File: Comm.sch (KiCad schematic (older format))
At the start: 12 parts

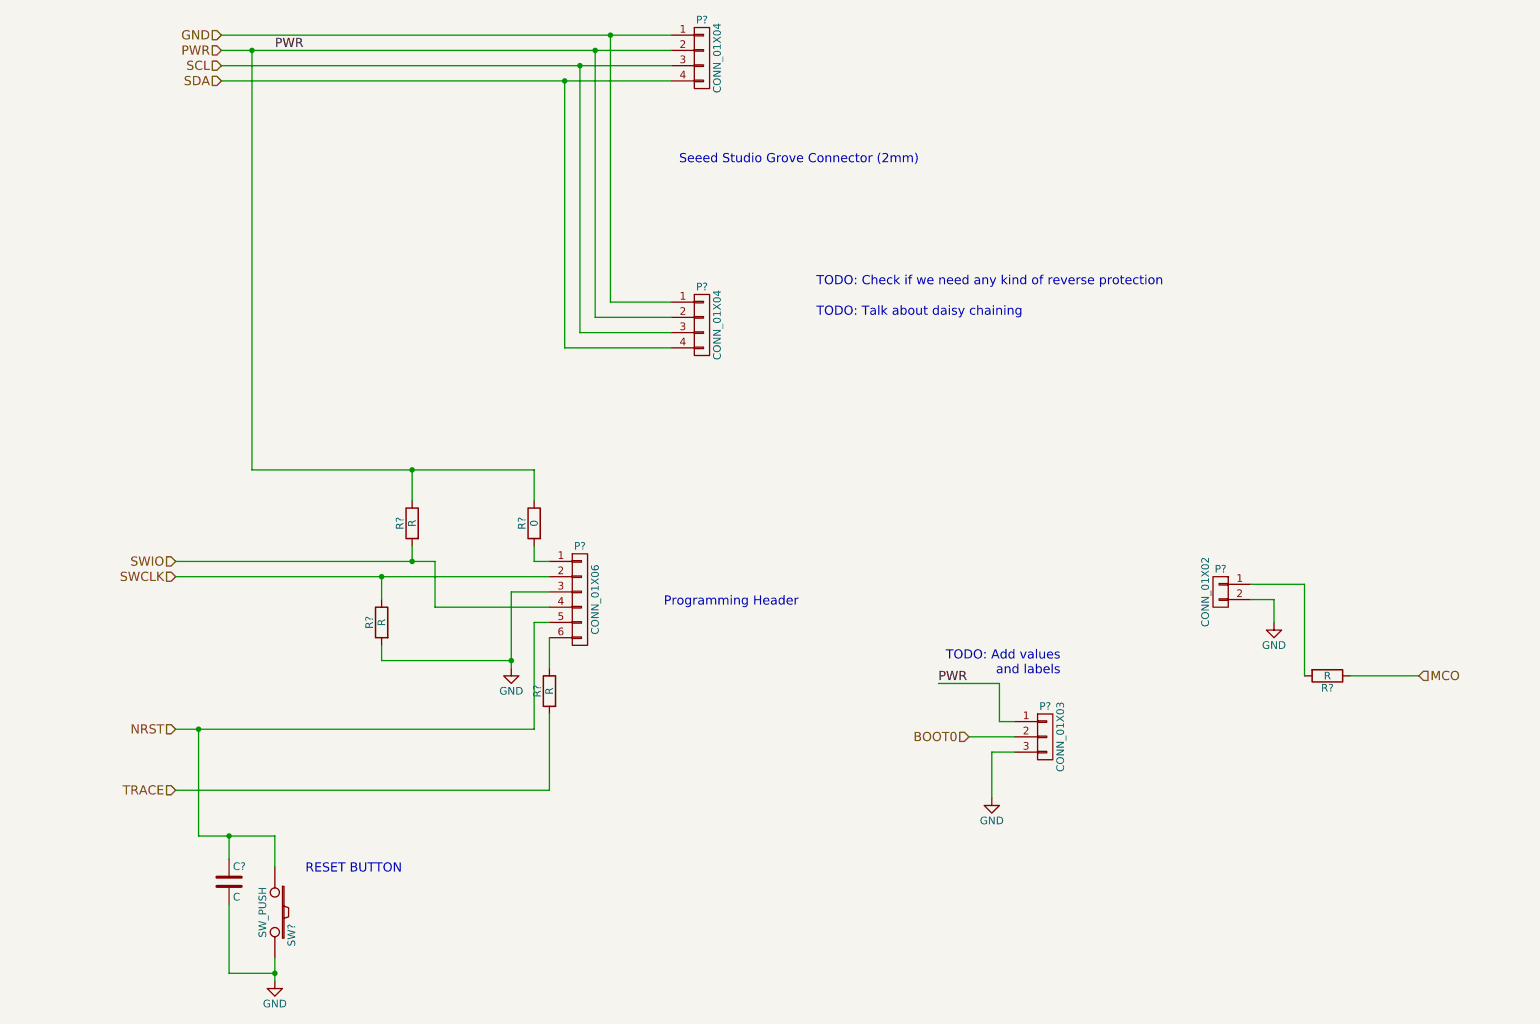
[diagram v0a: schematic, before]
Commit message: Associated footprints, created footprints for 2mm connector and did prelim placement
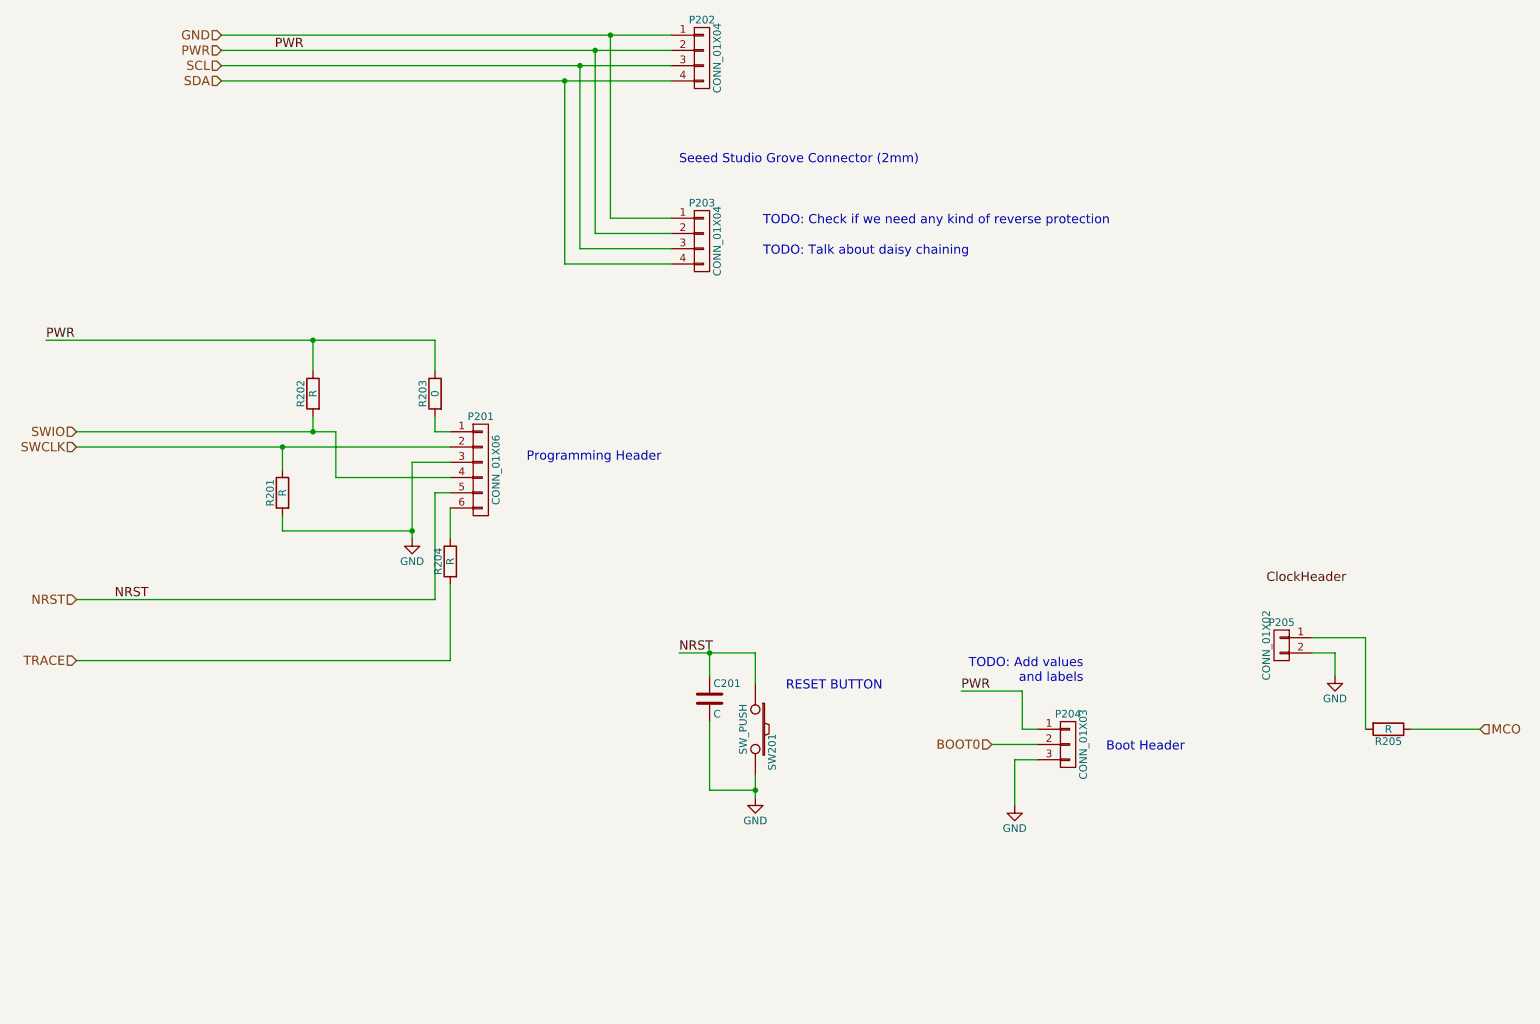
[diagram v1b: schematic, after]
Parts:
- C201: renamed from C?; footprint (none) -> Capacitors_SMD:C_0805
- P202, P203: renamed from P?; footprint (none) -> CentralCommand:Grove-2mm
- P204: renamed from P?; footprint (none) -> Pin_Headers:Pin_Header_Straight_1x03
- SW201: renamed from SW?; footprint (none) -> Buttons_Switches_ThroughHole:SW_PUSH_SMALL
- gave numbers to parts that had none: 7
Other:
- note added: "Boot Header"
- moved on the sheet: C201, P201, P203, P204, P205, R201, R202, R203, R204, R205, SW201

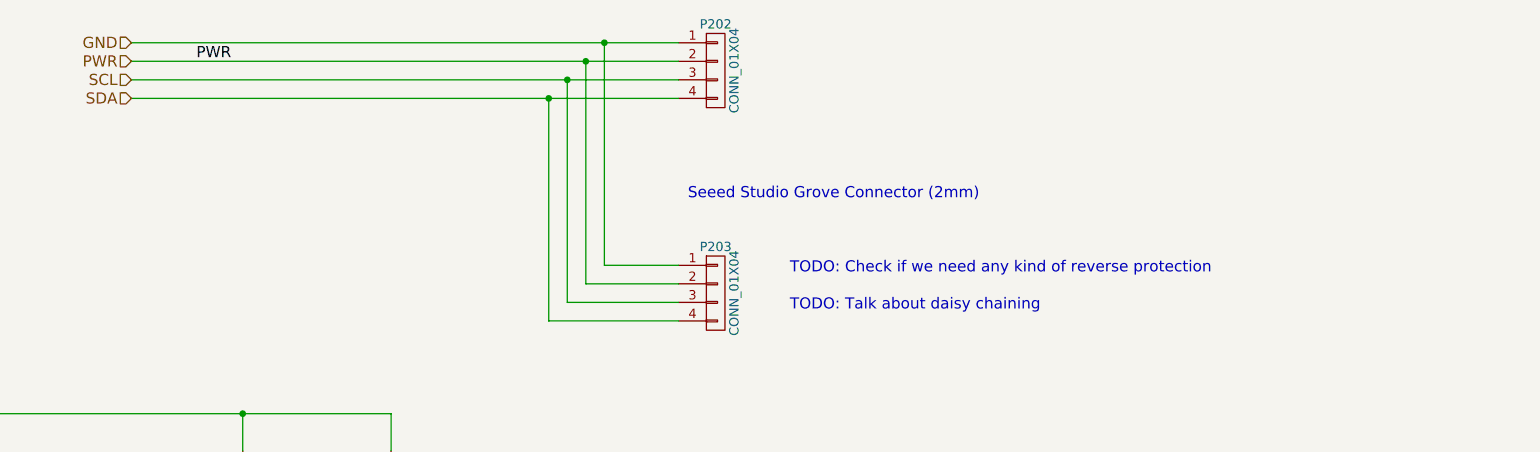
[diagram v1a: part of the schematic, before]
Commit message: Swapped connections on the Grove connector
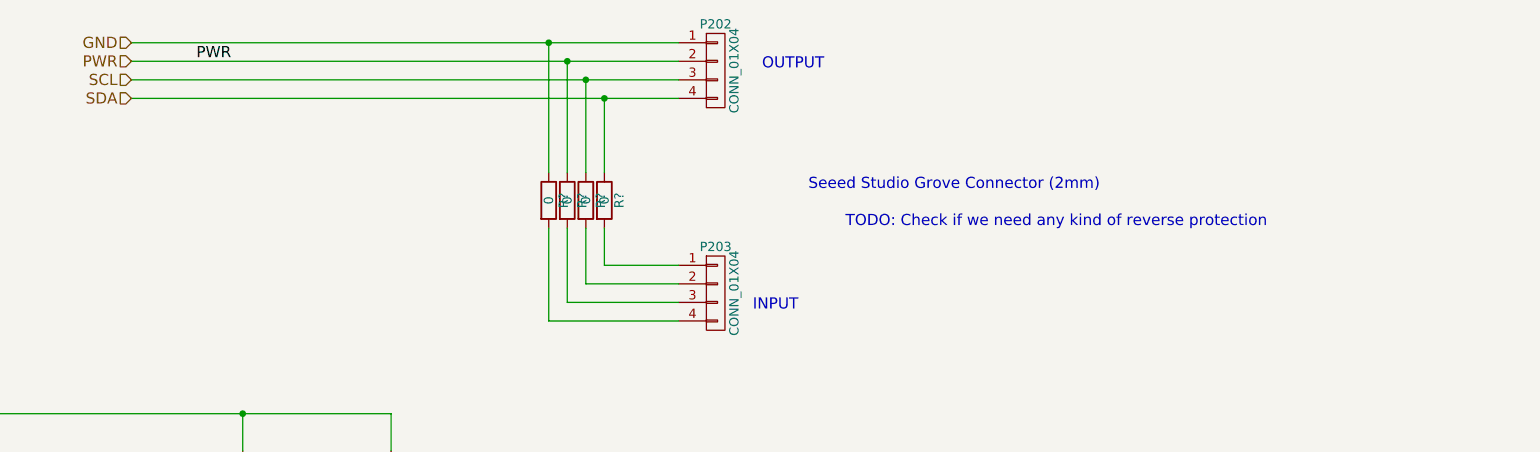
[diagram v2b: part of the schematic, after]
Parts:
- added R? (x4): 0, symbol R
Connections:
- net GND: now also R?.1; no longer P203.1 (P1)
- net PWR: now also R?.1; no longer P203.2 (P2)
- net SCL: now also R?.1; no longer P203.3 (P3)
- net SDA: now also R?.1; no longer P203.4 (P4)
- new net: P203.1 (P1), R?.2
- new net: P203.2 (P2), R?.2
- new net: P203.3 (P3), R?.2
- new net: P203.4 (P4), R?.2
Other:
- note added: "INPUT"
- note added: "OUTPUT"
- note removed: "TODO: Talk about daisy chaining"
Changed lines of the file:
@@
 SDA
 Wire Wire Line
-	2250 1500 5200 1500
-Wire Wire Line
-	2250 1400 5200 1400
-Wire Wire Line
-	2250 1300 5200 1300
-Wire Wire Line
-	2250 1200 5200 1200
-Wire Wire Line
-	4800 1200 4800 2400
-Wire Wire Line
 	4800 2400 5200 2400
-Connection ~ 4800 1200
-Wire Wire Line
-	4700 1300 4700 2500
 Wire Wire Line
 	4700 2500 5200 2500
-Connection ~ 4700 1300
-Wire Wire Line
-	4600 1400 4600 2600
 Wire Wire Line
 	4600 2600 5200 2600
-Connection ~ 4600 1400
 Wire Wire Line
 	5200 2700 4500 2700
-Wire Wire Line
-	4500 2700 4500 1500
-Connection ~ 4500 1500
-Text Notes 5250 2050 0    60   ~ 0
+Text Notes 5900 2000 0    60   ~ 0
 Seeed Studio Grove Connector (2mm)
-Text Notes 5800 2450 0    60   ~ 0
+Text Notes 6100 2200 0    60   ~ 0
 TODO: Check if we need any kind of reverse protection
-Text Notes 5800 2650 0    60   ~ 0
-TODO: Talk about daisy chaining
 $Comp
 L CONN_01X06 P201
@@
 Text Label 9100 4800 0    60   ~ 0
 ClockHeader
+Wire Wire Line
+	5200 1200 2250 1200
+Wire Wire Line
+	2250 1300 5200 1300
+Wire Wire Line
+	5200 1400 2250 1400
+Wire Wire Line
+	2250 1500 5200 1500
+$Comp
+L R R?
+U 1 1 56691488
+P 4800 2050
+F 0 "R?" V 4880 2050 50  0000 C CNN
+F 1 "0" V 4800 2050 50  0000 C CNN
+F 2 "" V 4730 2050 30  0000 C CNN
+F 3 "" H 4800 2050 30  0000 C CNN
+	1    4800 2050
+	1    0    0    -1
+$EndComp
+Wire Wire Line
+	4800 2200 4800 2400
+Wire Wire Line
+	4800 1900 4800 1500
+Connection ~ 4800 1500
+$Comp
+L R R?
+U 1 1 566915C1
+P 4700 2050
+F 0 "R?" V 4780 2050 50  0000 C CNN
+F 1 "0" V 4700 2050 50  0000 C CNN
+F 2 "" V 4630 2050 30  0000 C CNN
+F 3 "" H 4700 2050 30  0000 C CNN
+	1    4700 2050
+	1    0    0    -1
+$EndComp
+Wire Wire Line
+	4700 2500 4700 2200
+$Comp
+L R R?
+U 1 1 56691697
+P 4600 2050
+F 0 "R?" V 4680 2050 50  0000 C CNN
+F 1 "0" V 4600 2050 50  0000 C CNN
+F 2 "" V 4530 2050 30  0000 C CNN
+F 3 "" H 4600 2050 30  0000 C CNN
+	1    4600 2050
+	1    0    0    -1
+$EndComp
+Wire Wire Line
+	4600 2600 4600 2200
+Wire Wire Line
+	4600 1900 4600 1300
+Connection ~ 4600 1300
+Wire Wire Line
+	4700 1900 4700 1400
+Connection ~ 4700 1400
+$Comp
+L R R?
+U 1 1 56691864
+P 4500 2050
+F 0 "R?" V 4580 2050 50  0000 C CNN
+F 1 "0" V 4500 2050 50  0000 C CNN
+F 2 "" V 4430 2050 30  0000 C CNN
+F 3 "" H 4500 2050 30  0000 C CNN
+	1    4500 2050
+	1    0    0    -1
+$EndComp
+Wire Wire Line
+	4500 2700 4500 2200
+Wire Wire Line
+	4500 1900 4500 1200
+Connection ~ 4500 1200
+Text Notes 5650 1350 0    60   ~ 0
+OUTPUT
+Text Notes 5600 2650 0    60   ~ 0
+INPUT
 $EndSCHEMATC

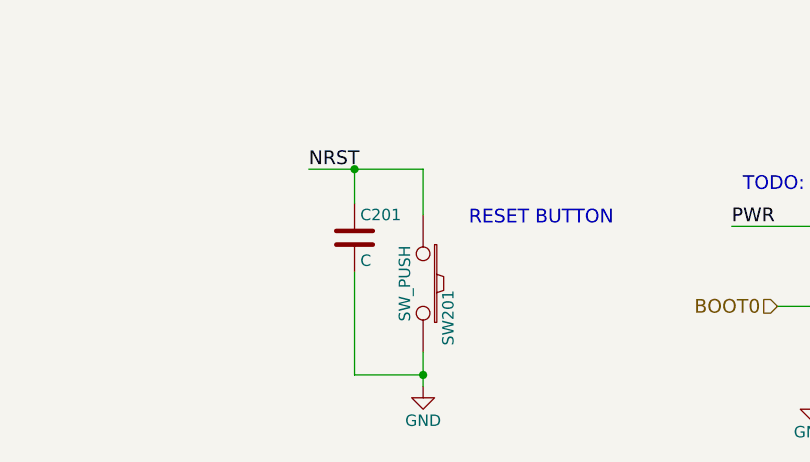
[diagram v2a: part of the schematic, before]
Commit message: Added ground and power layers.
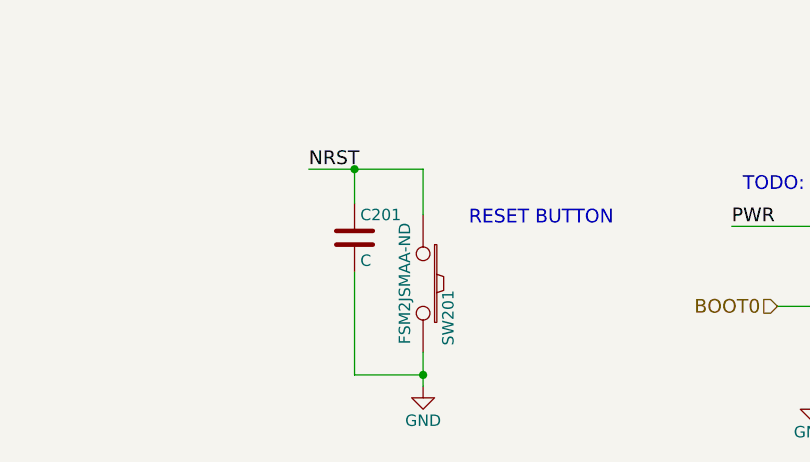
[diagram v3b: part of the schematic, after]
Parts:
- SW201: value SW_PUSH -> FSM2JSMAA-ND
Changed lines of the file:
@@
 P 5750 5750
 F 0 "SW201" H 5900 5860 50  0000 C CNN
-F 1 "SW_PUSH" H 5750 5670 50  0000 C CNN
+F 1 "FSM2JSMAA-ND" H 5750 5670 50  0000 C CNN
 F 2 "Buttons_Switches_ThroughHole:SW_PUSH_SMALL" H 5750 5750 60  0001 C CNN
-F 3 "" H 5750 5750 60  0000 C CNN
+F 3 "http://www.digikey.com/product-detail/en/FSM2JSMAA/FSM2JSMAA-ND/2400228" H 5750 5750 60  0001 C CNN
 	1    5750 5750
 	0    1    1    0

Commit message: Finished laying out power section
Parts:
- R206, R207, R208, R209: renamed from R?; footprint (none) -> Resistors_SMD:R_0805
- SW201: footprint Buttons_Switches_ThroughHole:SW_PUSH_SMALL -> CentralCommand:FSM2JSMAA-ND
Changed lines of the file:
@@
 $EndComp
 $Comp
-L GND #PWR04
+L GND #PWR05
 U 1 1 565FC7CA
 P 3500 4500
-F 0 "#PWR04" H 3500 4250 50  0001 C CNN
+F 0 "#PWR05" H 3500 4250 50  0001 C CNN
 F 1 "GND" H 3500 4350 50  0000 C CNN
 F 2 "" H 3500 4500 60  0000 C CNN
@@
 F 0 "SW201" H 5900 5860 50  0000 C CNN
 F 1 "FSM2JSMAA-ND" H 5750 5670 50  0000 C CNN
-F 2 "Buttons_Switches_ThroughHole:SW_PUSH_SMALL" H 5750 5750 60  0001 C CNN
+F 2 "CentralCommand:FSM2JSMAA-ND" H 5750 5750 60  0001 C CNN
 F 3 "http://www.digikey.com/product-detail/en/FSM2JSMAA/FSM2JSMAA-ND/2400228" H 5750 5750 60  0001 C CNN
 	1    5750 5750
@@
 $EndComp
 $Comp
-L GND #PWR05
+L GND #PWR06
 U 1 1 565FED52
 P 5750 6200
-F 0 "#PWR05" H 5750 5950 50  0001 C CNN
+F 0 "#PWR06" H 5750 5950 50  0001 C CNN
 F 1 "GND" H 5750 6050 50  0000 C CNN
 F 2 "" H 5750 6200 60  0000 C CNN
@@
 $EndComp
 $Comp
-L GND #PWR06
+L GND #PWR07
 U 1 1 5660DBDE
 P 9550 5400
-F 0 "#PWR06" H 9550 5150 50  0001 C CNN
+F 0 "#PWR07" H 9550 5150 50  0001 C CNN
 F 1 "GND" H 9550 5250 50  0000 C CNN
 F 2 "" H 9550 5400 60  0000 C CNN
@@
 	7450 5950 7450 6250
 $Comp
-L GND #PWR07
+L GND #PWR08
 U 1 1 5661772D
 P 7450 6250
-F 0 "#PWR07" H 7450 6000 50  0001 C CNN
+F 0 "#PWR08" H 7450 6000 50  0001 C CNN
 F 1 "GND" H 7450 6100 50  0000 C CNN
 F 2 "" H 7450 6250 60  0000 C CNN
@@
 	2250 1500 5200 1500
 $Comp
-L R R?
+L R R209
 U 1 1 56691488
 P 4800 2050
-F 0 "R?" V 4880 2050 50  0000 C CNN
+F 0 "R209" V 4880 2050 50  0000 C CNN
 F 1 "0" V 4800 2050 50  0000 C CNN
-F 2 "" V 4730 2050 30  0000 C CNN
+F 2 "Resistors_SMD:R_0805" V 4730 2050 30  0001 C CNN
 F 3 "" H 4800 2050 30  0000 C CNN
 	1    4800 2050
@@
 Connection ~ 4800 1500
 $Comp
-L R R?
+L R R208
 U 1 1 566915C1
 P 4700 2050
-F 0 "R?" V 4780 2050 50  0000 C CNN
+F 0 "R208" V 4780 2050 50  0000 C CNN
 F 1 "0" V 4700 2050 50  0000 C CNN
-F 2 "" V 4630 2050 30  0000 C CNN
+F 2 "Resistors_SMD:R_0805" V 4630 2050 30  0001 C CNN
 F 3 "" H 4700 2050 30  0000 C CNN
 	1    4700 2050
@@
 	4700 2500 4700 2200
 $Comp
-L R R?
+L R R207
 U 1 1 56691697
 P 4600 2050
-F 0 "R?" V 4680 2050 50  0000 C CNN
+F 0 "R207" V 4680 2050 50  0000 C CNN
 F 1 "0" V 4600 2050 50  0000 C CNN
-F 2 "" V 4530 2050 30  0000 C CNN
+F 2 "Resistors_SMD:R_0805" V 4530 2050 30  0001 C CNN
 F 3 "" H 4600 2050 30  0000 C CNN
 	1    4600 2050
@@
 Connection ~ 4700 1400
 $Comp
-L R R?
+L R R206
 U 1 1 56691864
 P 4500 2050
-F 0 "R?" V 4580 2050 50  0000 C CNN
+F 0 "R206" V 4580 2050 50  0000 C CNN
 F 1 "0" V 4500 2050 50  0000 C CNN
-F 2 "" V 4430 2050 30  0000 C CNN
+F 2 "Resistors_SMD:R_0805" V 4430 2050 30  0001 C CNN
 F 3 "" H 4500 2050 30  0000 C CNN
 	1    4500 2050

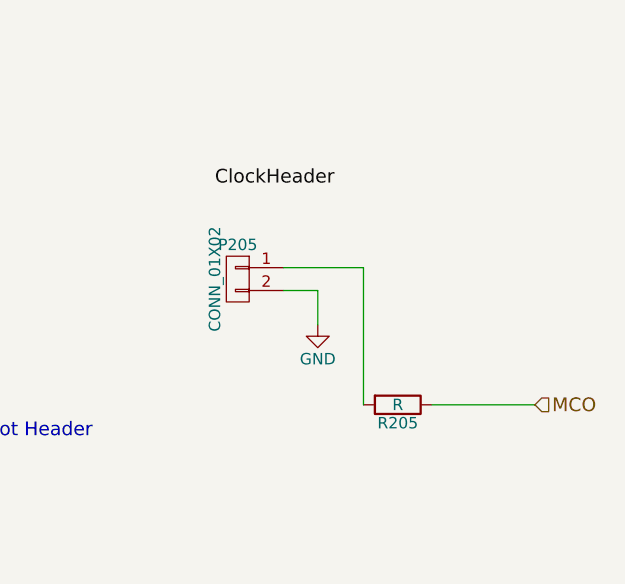
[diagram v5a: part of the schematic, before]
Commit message: Removed one header and finished connecting all parts
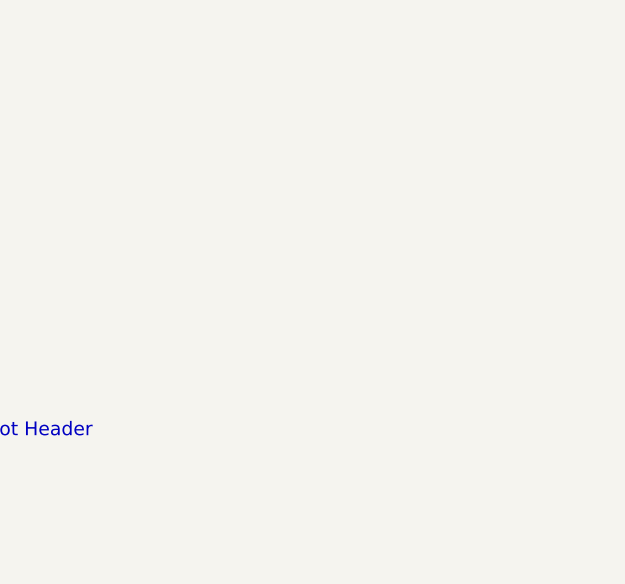
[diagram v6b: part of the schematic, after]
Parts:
- removed P205: CONN_01X02, Pin_Headers:Pin_Header_Straight_1x02, symbol CONN_01X02
- removed R205: R, Resistors_SMD:R_0805, symbol R
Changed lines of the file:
@@
 Text Notes 5950 5500 0    60   ~ 0
 RESET BUTTON
-$Comp
-L R R205
-U 1 1 5660DBD0
-P 9900 5750
-F 0 "R205" V 9980 5750 50  0000 C CNN
-F 1 "R" V 9900 5750 50  0000 C CNN
-F 2 "Resistors_SMD:R_0805" V 9830 5750 30  0001 C CNN
-F 3 "" H 9900 5750 30  0000 C CNN
-	1    9900 5750
-	0    1    1    0
-$EndComp
-$Comp
-L CONN_01X02 P205
-U 1 1 5660DBD7
-P 9200 5200
-F 0 "P205" H 9200 5350 50  0000 C CNN
-F 1 "CONN_01X02" V 9300 5200 50  0000 C CNN
-F 2 "Pin_Headers:Pin_Header_Straight_1x02" H 9200 5200 60  0001 C CNN
-F 3 "" H 9200 5200 60  0000 C CNN
-	1    9200 5200
-	-1   0    0    -1
-$EndComp
-$Comp
-L GND #PWR08
-U 1 1 5660DBDE
-P 9550 5400
-F 0 "#PWR08" H 9550 5150 50  0001 C CNN
-F 1 "GND" H 9550 5250 50  0000 C CNN
-F 2 "" H 9550 5400 60  0000 C CNN
-F 3 "" H 9550 5400 60  0000 C CNN
-	1    9550 5400
-	1    0    0    -1
-$EndComp
-Wire Wire Line
-	9750 5750 9750 5150
-Wire Wire Line
-	9750 5150 9400 5150
-Wire Wire Line
-	9400 5250 9550 5250
-Wire Wire Line
-	9550 5250 9550 5400
-Wire Wire Line
-	10050 5750 10500 5750
-Text HLabel 10500 5750 2    60   Input ~ 0
-MCO
 Text Notes 7900 5450 2    60   ~ 0
 TODO: Add values \nand labels
@@
 Text Notes 8050 5900 0    60   ~ 0
 Boot Header
-Text Label 9100 4800 0    60   ~ 0
-ClockHeader
 Wire Wire Line
 	5200 1200 2250 1200
